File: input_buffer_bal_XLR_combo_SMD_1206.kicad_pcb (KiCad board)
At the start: 2 copper layers, 62.5 x 55 mm, 31 parts, among them J1 CH1, J2 CH2, J3 POWER, J4 CH1_OUT, J5 CH2_OUT, U1 LM4562, U2 LM4562

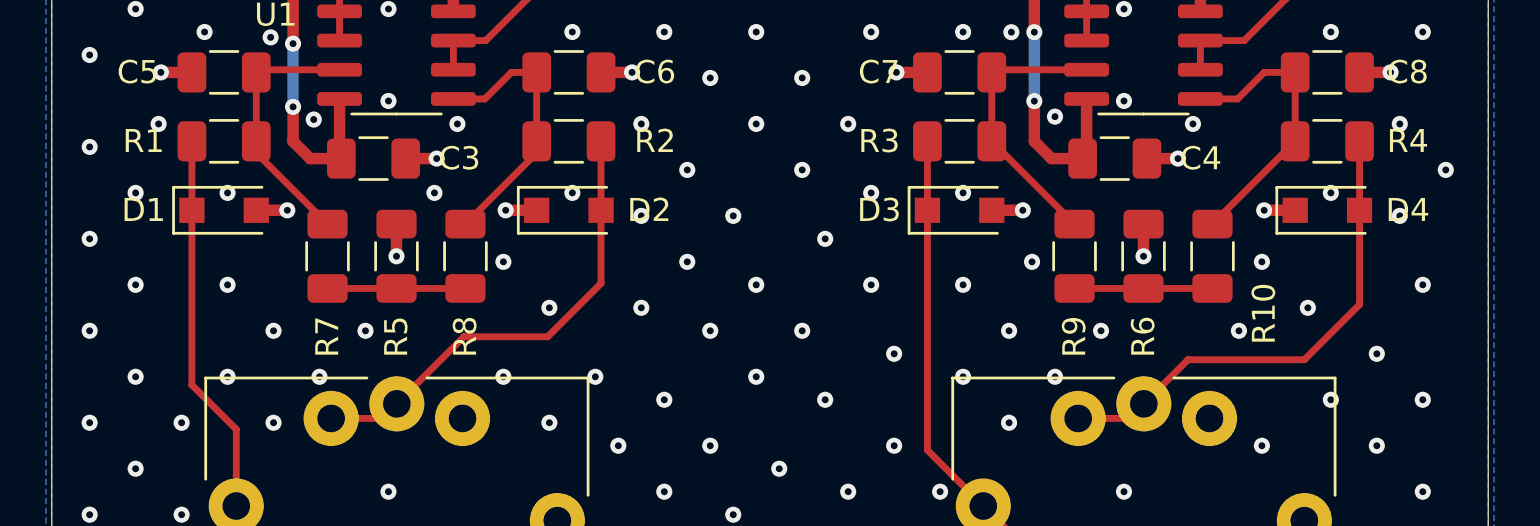
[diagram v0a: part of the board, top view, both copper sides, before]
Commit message: Changed footprint for TVS diodes to DFN1006
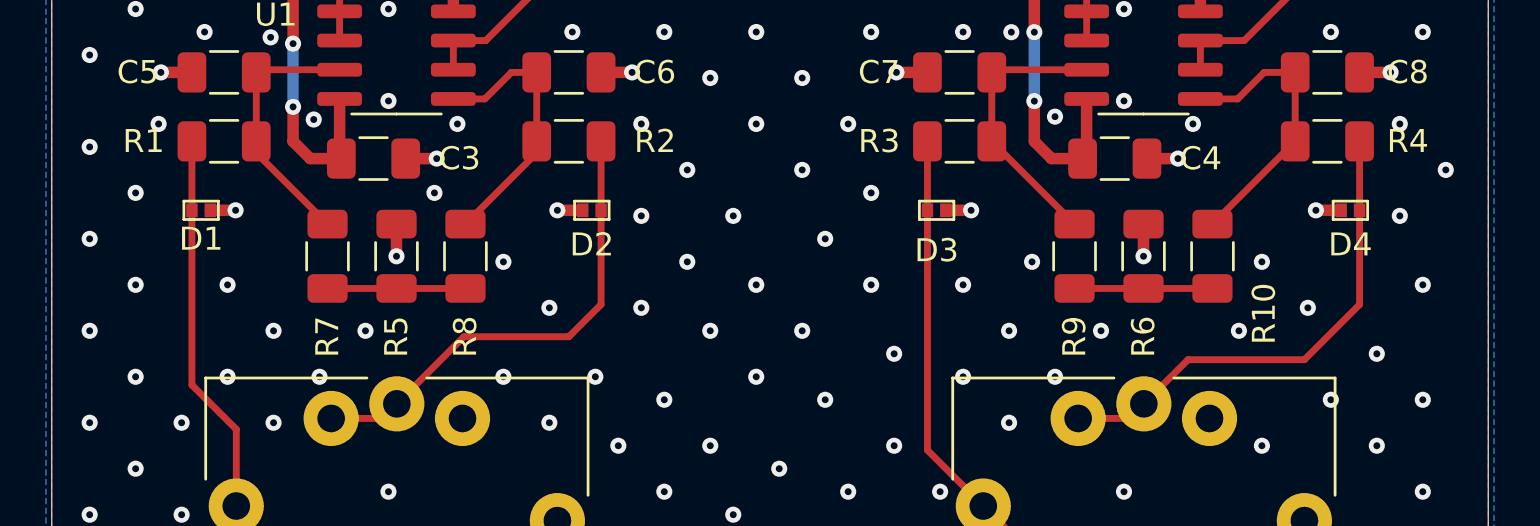
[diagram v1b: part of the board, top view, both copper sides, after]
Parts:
- D1, D2, D3, D4: footprint Diode_SMD:D_SOD-123F -> local_footprint_lib:D_DFN1006
- moved D1 1.00 mm to (96.5, 128.2)
- moved D2 1.00 mm to (113.5, 128.2)
- moved D3 1.00 mm to (128.5, 128.2)
- moved D4 1.00 mm to (146.5, 128.2)
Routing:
- net GND: track 18.9 -> 17.9 mm, vias 259 -> 255
- net Net-(D2-Pad2): track 20.4 -> 20.9 mm
